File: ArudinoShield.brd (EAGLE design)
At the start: 160 x 100 mm, 27 parts, among them IC1 L298, IC3 REG1117

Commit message: renamed component, updated ignore
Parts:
- renumbered IC3 to VREG
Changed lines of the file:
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@@
 </element>
 <element name="EN" library="con-amp" library_urn="urn:adsk.eagle:library:127" package="1X2MTA" package3d_urn="urn:adsk.eagle:package:8081562/1" value="" x="69.85" y="73.66" smashed="yes" rot="R180">
-<attribute name="NAME" x="74.2188" y="80.01" size="1.778" layer="25" rot="R180"/>
+<attribute name="NAME" x="78.0288" y="77.47" size="1.778" layer="25" rot="R180"/>
 <attribute name="POPULARITY" value="4" x="118.11" y="135.89" size="1.778" layer="27" rot="R180" display="off"/>
 <attribute name="VALUE" x="73.2869" y="69.2452" size="1.27" layer="27" rot="R180"/>
@@
 <attribute name="VALUE" x="77.851" y="31.75" size="1.27" layer="27" ratio="10" rot="R90"/>
 </element>
-<element name="IC3" library="burr-brown" library_urn="urn:adsk.eagle:library:111" package="SOT223" package3d_urn="urn:adsk.eagle:package:4940/1" value="REG1117" x="44.45" y="26.67" smashed="yes">
+<element name="VREG" library="burr-brown" library_urn="urn:adsk.eagle:library:111" package="SOT223" package3d_urn="urn:adsk.eagle:package:4940/1" value="REG1117" x="44.45" y="26.67" smashed="yes">
 <attribute name="MF" value="" x="-43.18" y="-64.77" size="1.778" layer="27" display="off"/>
 <attribute name="MPN" value="REG1117" x="-43.18" y="-64.77" size="1.778" layer="27" display="off"/>
@@
 <contactref element="C2" pad="1"/>
 <contactref element="JP1" pad="2"/>
-<contactref element="IC3" pad="2"/>
+<contactref element="VREG" pad="2"/>
 <wire x1="48.26" y1="41.91" x2="54.61" y2="66.04" width="0" layer="19" extent="1-1"/>
 <wire x1="44.4754" y1="23.5204" x2="48.26" y2="41.91" width="0" layer="19" extent="1-1"/>
@@
 <signal name="N$27">
 <contactref element="J2" pad="2"/>
-<contactref element="IC3" pad="3"/>
+<contactref element="VREG" pad="3"/>
 <wire x1="46.7614" y1="23.5204" x2="48.9712" y2="71.12" width="0" layer="19" extent="1-1"/>
 </signal>
@@
 <contactref element="D6" pad="A"/>
 <contactref element="C1" pad="2"/>
-<contactref element="IC3" pad="1"/>
+<contactref element="VREG" pad="1"/>
 <wire x1="62.23" y1="40.64" x2="54.61" y2="71.12" width="0" layer="19" extent="1-1"/>
 <wire x1="53.34" y1="35.56" x2="62.23" y2="40.64" width="0" layer="19" extent="1-1"/>

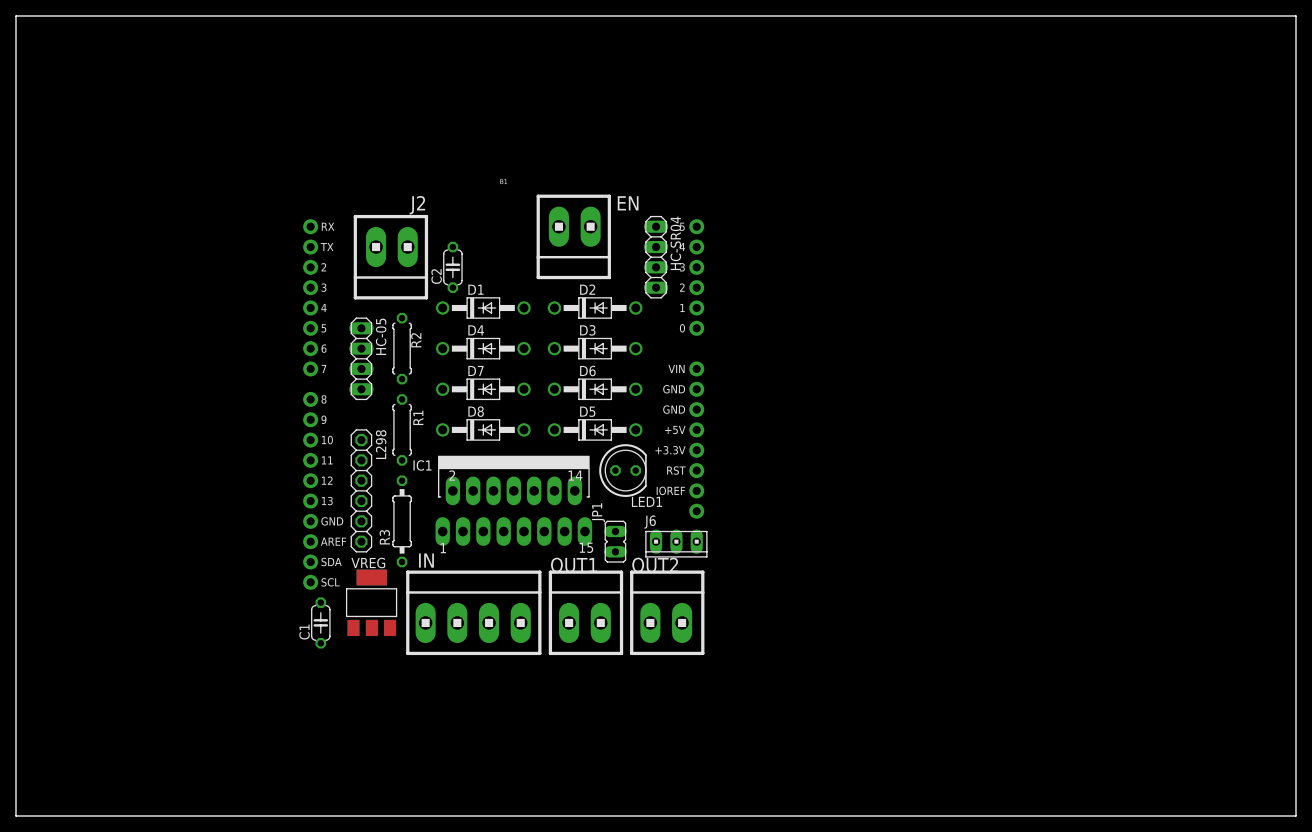
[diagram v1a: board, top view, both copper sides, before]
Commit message: added routes to board
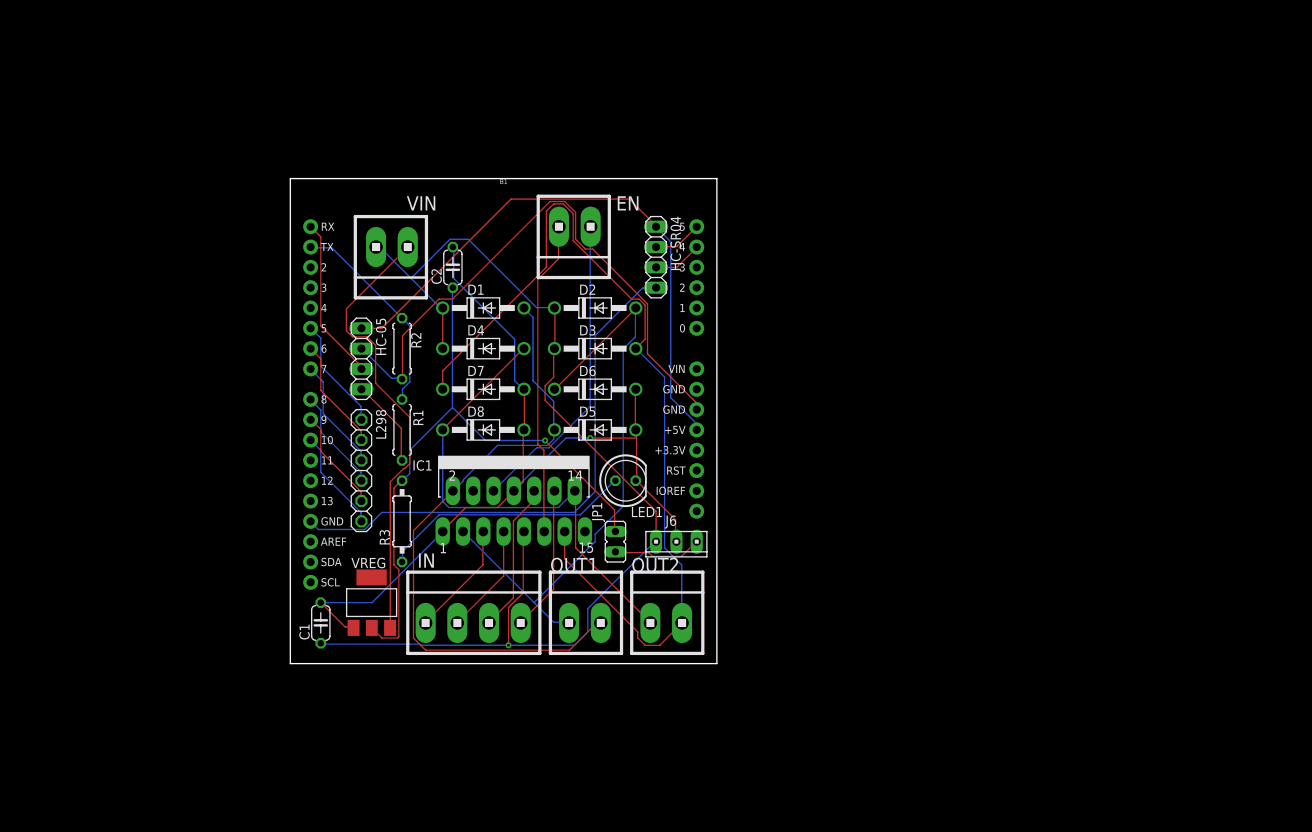
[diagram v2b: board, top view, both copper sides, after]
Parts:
- moved L298 2.54 mm to (43.2, 43.2)
- moved LED1 1.27 mm to (76.2, 41.9)
- renumbered J2 to VIN
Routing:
- net N$31: track 0.00 -> 139.8 mm, vias 0 -> 1
- net N$17: track 0.00 -> 114.3 mm
- net N$29: track 0.00 -> 109.8 mm, vias 0 -> 1
- net N$26: track 0.00 -> 79.3 mm, vias 0 -> 1
- net N$15: track 0.00 -> 79.3 mm
- net N$16: track 0.00 -> 74.5 mm
- net N$13: track 0.00 -> 72.7 mm
- net N$10: track 0.00 -> 72.5 mm
- net N$9: track 0.00 -> 67.6 mm
- net N$18: track 0.00 -> 61.5 mm
- net N$27: track 0.00 -> 56.2 mm
- net N$20: track 0.00 -> 39.5 mm
- net N$19: track 0.00 -> 38.9 mm
- net N$25: track 0.00 -> 31.6 mm
- net N$11: track 0.00 -> 26.1 mm
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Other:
- board size 160 x 100 mm -> 53.3 x 60.6 mm

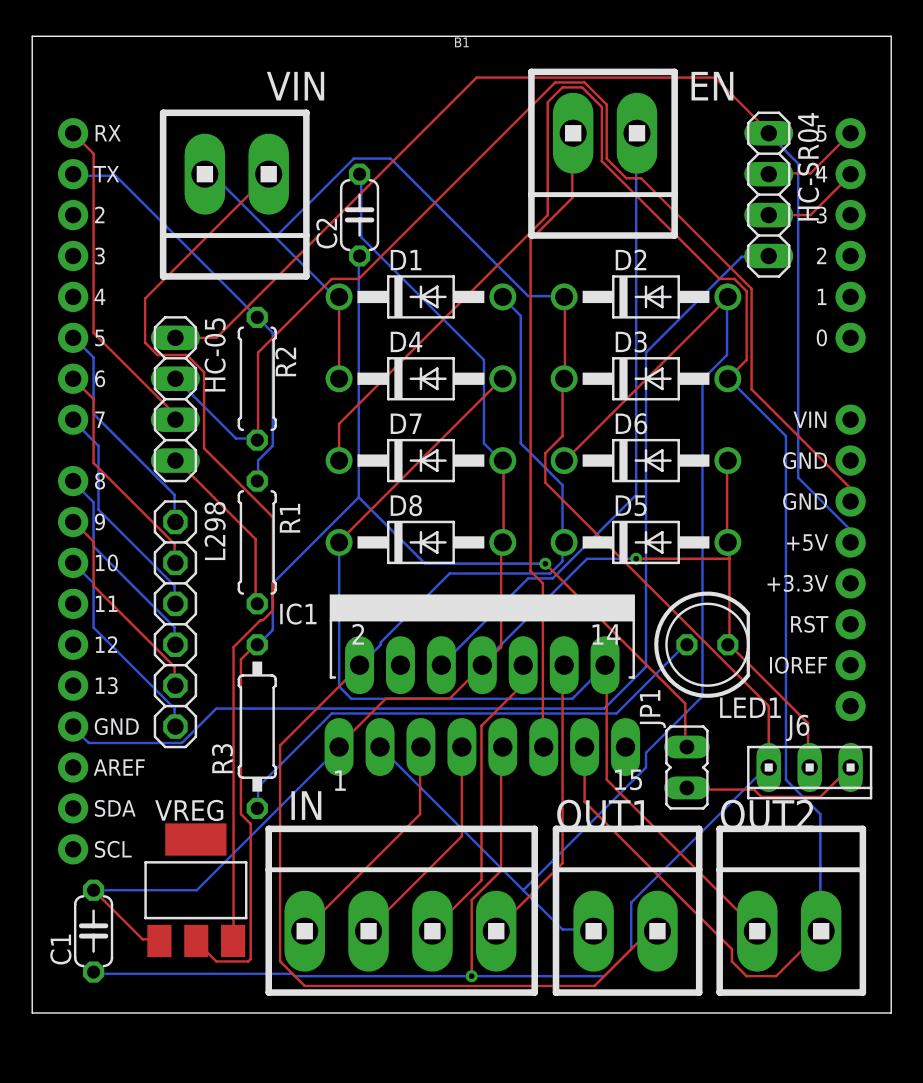
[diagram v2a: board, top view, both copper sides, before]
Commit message: reduced schematic
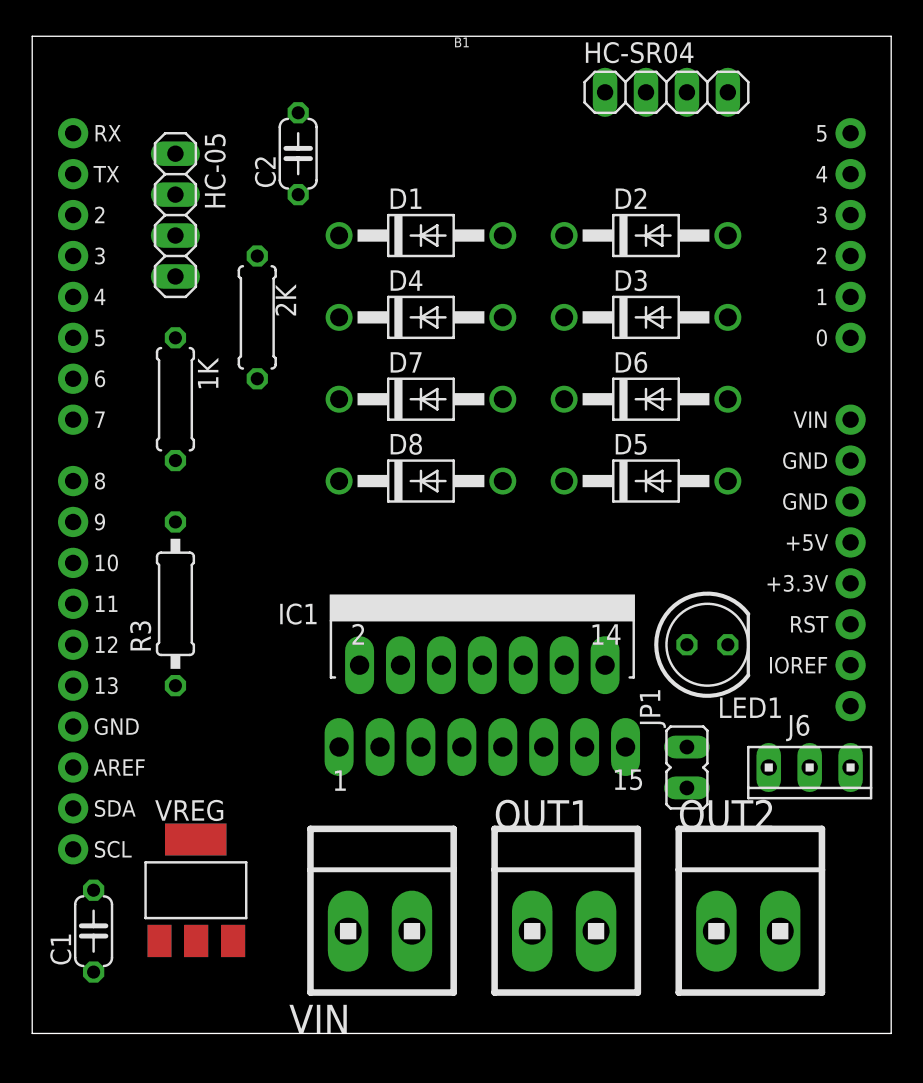
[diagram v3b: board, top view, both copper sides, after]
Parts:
- removed EN: (no value), con-amp:1X2MTA
- removed IN: (no value), con-amp:1X4MTA
- removed L298: (no value), adafruit:1X06
- removed R1, R2: (no value), adafruit:0207/7
- added 1K, 2K: (no value), adafruit:0207/7
- moved VIN 47.8 mm to (55.9, 24.1), turned to 0 degrees
- moved HC-05 11.4 mm to (43.2, 68.6)
- moved R3 9.16 mm to (43.2, 44.5)
- moved HC-SR04 8.98 mm to (73.7, 76.2), turned to 0 degrees
- moved C2 5.39 mm to (50.8, 72.4)
- moved D1 3.81 mm to (58.4, 67.3)
- moved D2 3.81 mm to (72.4, 67.3)
- moved D5 3.81 mm to (72.4, 52.1)
- moved D8 3.81 mm to (58.4, 52.1)
- moved OUT1 3.81 mm to (67.3, 24.1)
- moved D3 3.81 mm to (72.4, 62.2)
- moved D4 3.81 mm to (58.4, 62.2)
- moved D6 3.81 mm to (72.4, 57.1)
- moved D7 3.81 mm to (58.4, 57.1)
- moved OUT2 2.54 mm to (78.7, 24.1)
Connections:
- removed net N$19: EN.2, IC1.6
- removed net N$23: IC1.10, IN.2
- removed net N$3: B1.D7, L298.3
- removed net N$4: B1.D8, L298.4
- removed net N$5: B1.D9, L298.5
- removed net N$6: B1.D10, L298.6
- net N$1: now also IC1.6; no longer L298.1
- net N$11: now also 1K.1, 2K.2; no longer R1.1, R2.2
- net N$13: now also 2K.1; no longer R2.1
- net N$14: now also 1K.2; no longer R1.2
- net N$2: now also B1.D8, IC1.10; no longer B1.D6, L298.2
- net N$20: now also B1.D10; no longer EN.1
- net N$21: now also B1.D6; no longer IN.4
- net N$22: now also B1.D7; no longer IN.3
- net N$24: now also B1.D9; no longer IN.1
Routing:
- net N$31: track 139.8 -> 0.00 mm, vias 1 -> 0
- net N$17: track 114.3 -> 0.00 mm
- net N$29: track 109.8 -> 0.00 mm, vias 1 -> 0
- net N$26: track 79.3 -> 0.00 mm, vias 1 -> 0
- net N$15: track 79.3 -> 0.00 mm
- net N$16: track 74.5 -> 0.00 mm
- net N$13: track 72.7 -> 0.00 mm
- net N$10: track 72.5 -> 0.00 mm
- net N$9: track 67.6 -> 0.00 mm
- net N$18: track 61.5 -> 0.00 mm
- net N$27: track 56.2 -> 0.00 mm
- net N$20: track 39.5 -> 0.00 mm
- net N$19: track 38.9 -> 0.00 mm
- net N$25: track 31.6 -> 0.00 mm
- net N$11: track 26.1 -> 0.00 mm
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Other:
- board size 53.3 x 60.6 mm -> 53.3 x 61.9 mm

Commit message: Reduced shield schematic
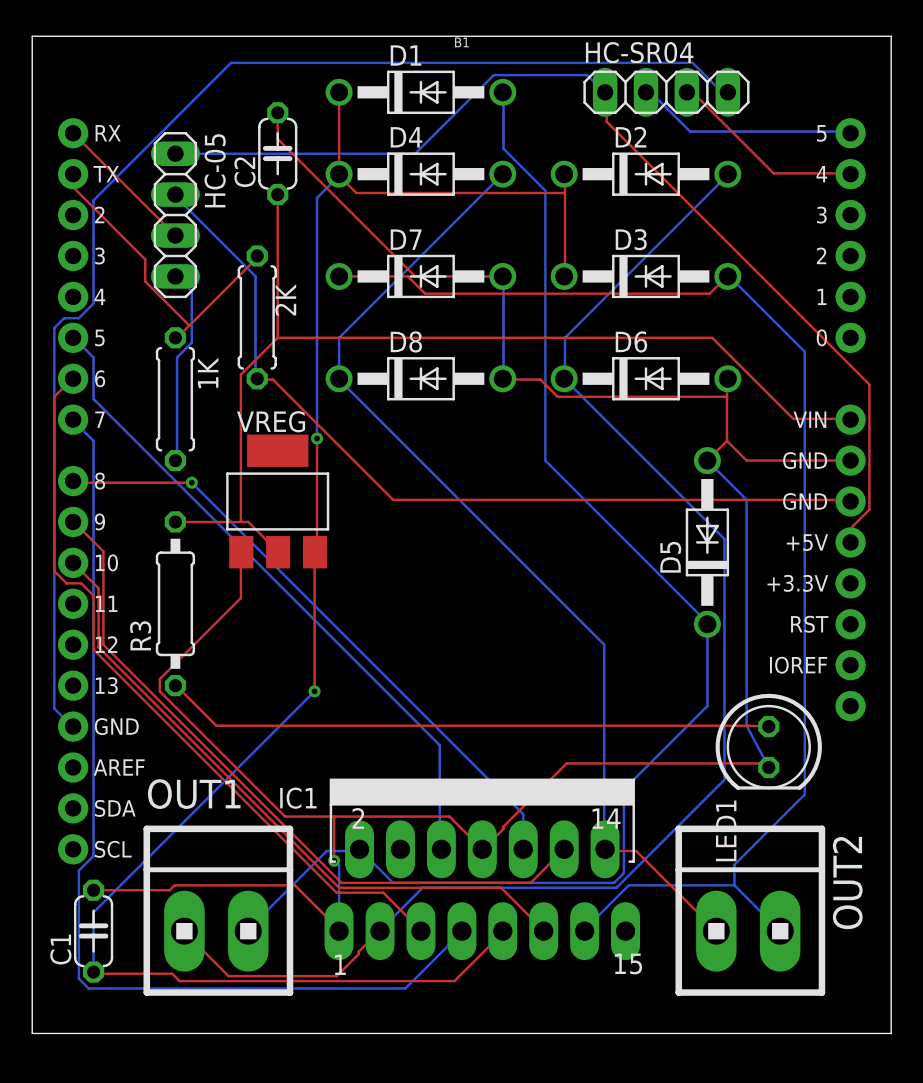
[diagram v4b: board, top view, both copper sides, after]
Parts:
- removed J6: (no value), con-amp:10X03MTA
- removed JP1: (no value), jumper:JP1
- removed VIN: (no value), con-amp:1X2MTA
- moved VREG 24.7 mm to (49.5, 50.8)
- moved OUT1 21.6 mm to (45.7, 24.1)
- moved IC1 11.4 mm to (62.2, 31.8)
- moved D4 8.89 mm to (58.4, 71.1)
- moved D1 8.89 mm to (58.4, 76.2)
- moved D7 7.62 mm to (58.4, 64.8)
- moved LED1 7.41 mm to (80.0, 35.6), turned to 270 degrees
- moved D8 6.35 mm to (58.4, 58.4)
- moved D5 5.39 mm to (76.2, 48.3), turned to 90 degrees
- moved D2 3.81 mm to (72.4, 71.1)
- moved D3 2.54 mm to (72.4, 64.8)
- moved D6 1.27 mm to (72.4, 58.4)
- moved C2 1.27 mm to (49.5, 72.4)
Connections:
- net N$28 renamed VS
- removed net N$27: VIN.2, VREG.3
- removed net N$30: J6.3, JP1.1
- net N$26: now also B1.VIN; no longer JP1.2
- net N$29: now also B1.GND@1; no longer J6.2
- net N$31: now also VREG.3; no longer J6.1, VIN.1
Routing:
- net N$29: track 0.00 -> 152.9 mm, vias 0 -> 1
- net N$31: track 0.00 -> 109.0 mm, vias 0 -> 2
- net N$16: track 0.00 -> 85.8 mm
- net N$15: track 0.00 -> 82.5 mm
- net N$17: track 0.00 -> 81.2 mm
- net N$9: track 0.00 -> 78.4 mm
- net N$26: track 0.00 -> 66.1 mm
- net N$10: track 0.00 -> 64.4 mm
- net N$18: track 0.00 -> 62.0 mm
- net N$22: track 0.00 -> 61.1 mm
- net N$13: track 0.00 -> 53.6 mm
- net N$21: track 0.00 -> 46.4 mm
- net N$24: track 0.00 -> 44.0 mm
- net N$1: track 0.00 -> 41.3 mm
- net N$20: track 0.00 -> 40.8 mm
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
